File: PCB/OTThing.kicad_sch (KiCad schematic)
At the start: 68 parts, among them IC1 TPS61041, J3 USB_C_Receptacle_USB2.0, Q13 BC847C, SW1 RST/CONFIG, SW2 BOOT, U1 ESP32-C3-WROOM-02, U5 USBLC6-2SC6, U6 AMS1117-3.3

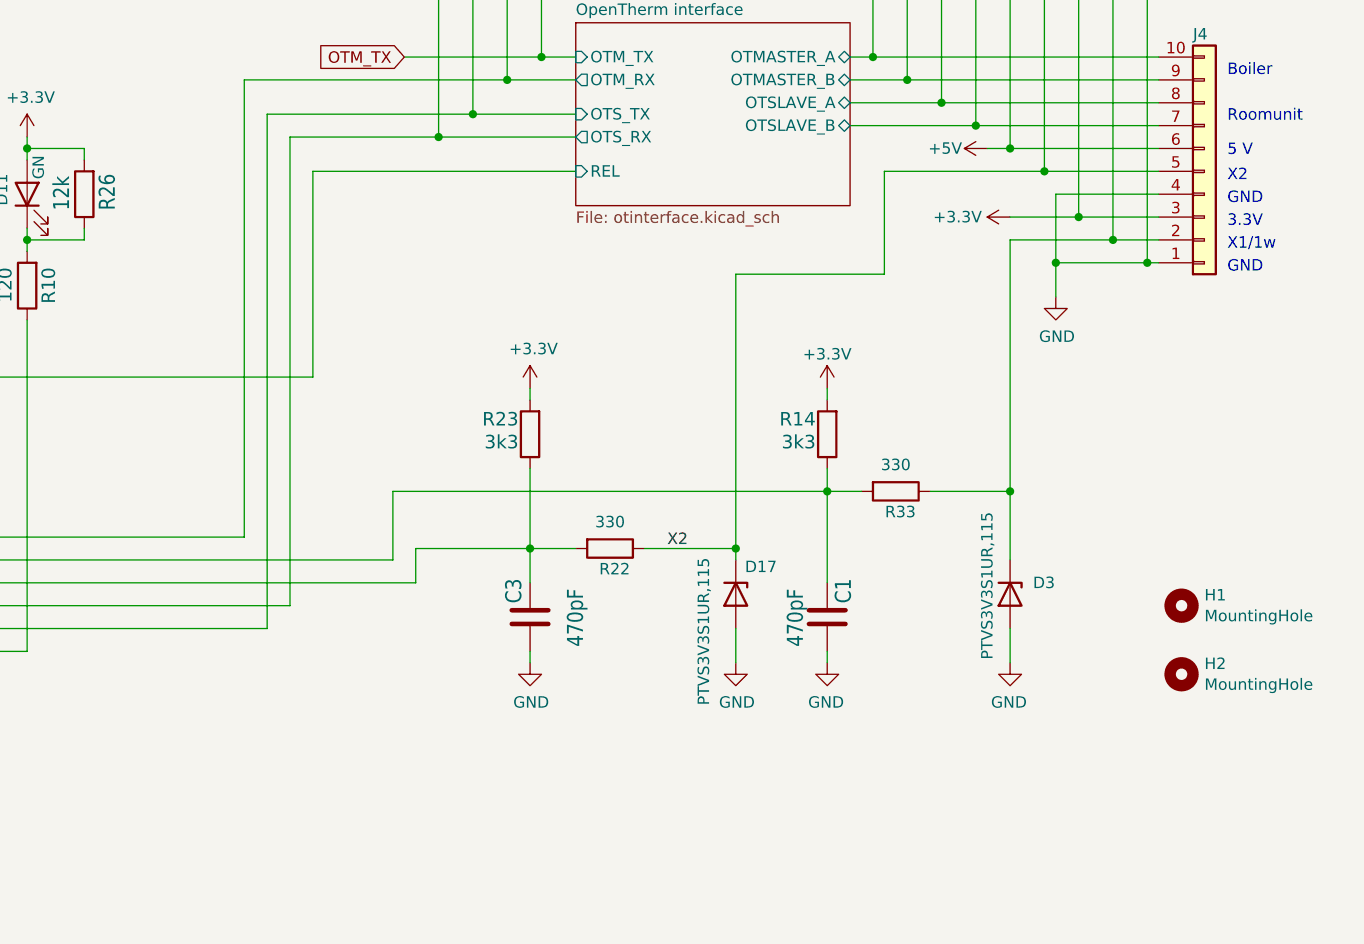
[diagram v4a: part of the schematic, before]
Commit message: add fiducals
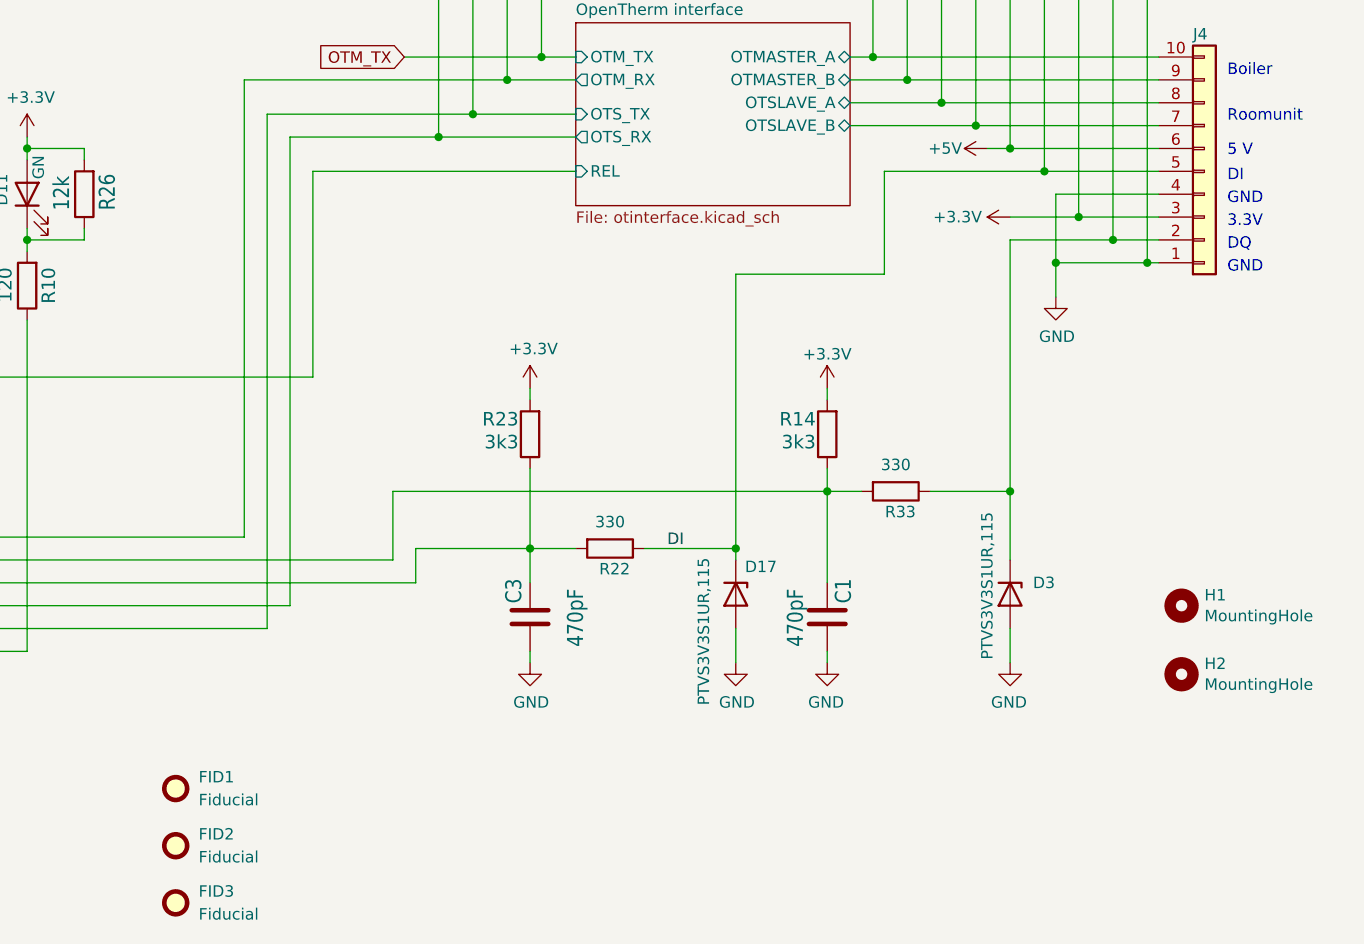
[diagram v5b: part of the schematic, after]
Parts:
- added FID1, FID2, FID3: Fiducial, Fiducial:Fiducial_0.5mm_Mask1.5mm, symbol Mechanical:Fiducial
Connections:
- net X2 renamed DI
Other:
- note added: "DI"
- note added: "DQ"
- note removed: "X1/1w"
- note removed: "X2"
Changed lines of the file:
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@@
 		)
 	)
-	(text "X1/1w"
+	(text "DQ"
 		(exclude_from_sim no)
 		(at 271.78 114.3 0)
@@
 		)
 	)
-	(text "X2"
+	(text "DI"
 		(exclude_from_sim no)
 		(at 271.78 106.68 0)
@@
 		)
 	)
-	(label "X2"
+	(label "DI"
 		(at 209.55 147.32 0)
 		(effects
@@
 	)
 	(symbol
+		(lib_id "Mechanical:Fiducial")
+		(at 154.94 173.99 0)
+		(unit 1)
+		(exclude_from_sim no)
+		(in_bom no)
+		(on_board yes)
+		(dnp no)
+		(fields_autoplaced yes)
+		(property "Reference" "FID1"
+			(at 157.48 172.7199 0)
+			(effects
+				(font
+					(size 1.27 1.27)
+				)
+				(justify left)
+			)
+		)
+		(property "Value" "Fiducial"
+			(at 157.48 175.2599 0)
+			(effects
+				(font
+					(size 1.27 1.27)
+				)
+				(justify left)
+			)
+		)
+		(property "Footprint" "Fiducial:Fiducial_0.5mm_Mask1.5mm"
+			(at 154.94 173.99 0)
+			(effects
+				(font
+					(size 1.27 1.27)
+				)
+				(hide yes)
+			)
+		)
+		(property "Datasheet" "~"
+			(at 154.94 173.99 0)
+			(effects
+				(font
+					(size 1.27 1.27)
+				)
+				(hide yes)
+			)
+		)
+		(property "Description" "Fiducial Marker"
+			(at 154.94 173.99 0)
+			(effects
+				(font
+					(size 1.27 1.27)
+				)
+				(hide yes)
+			)
+		)
+		(instances
+			(project ""
+				(path "/cb61f12f-ab02-48e5-a06c-10aea7e452c9"
+					(reference "FID1")
+					(unit 1)
+				)
+			)
+		)
+	)
+	(symbol
 		(lib_id "power:+3.3V")
 		(at 227.33 129.54 0)
@@
 	)
 	(symbol
+		(lib_id "Mechanical:Fiducial")
+		(at 154.94 186.69 0)
+		(unit 1)
+		(exclude_from_sim no)
+		(in_bom no)
+		(on_board yes)
+		(dnp no)
+		(fields_autoplaced yes)
+		(property "Reference" "FID3"
+			(at 157.48 185.4199 0)
+			(effects
+				(font
+					(size 1.27 1.27)
+				)
+				(justify left)
+			)
+		)
+		(property "Value" "Fiducial"
+			(at 157.48 187.9599 0)
+			(effects
+				(font
+					(size 1.27 1.27)
+				)
+				(justify left)
+			)
+		)
+		(property "Footprint" "Fiducial:Fiducial_0.5mm_Mask1.5mm"
+			(at 154.94 186.69 0)
+			(effects
+				(font
+					(size 1.27 1.27)
+				)
+				(hide yes)
+			)
+		)
+		(property "Datasheet" "~"
+			(at 154.94 186.69 0)
+			(effects
+				(font
+					(size 1.27 1.27)
+				)
+				(hide yes)
+			)
+		)
+		(property "Description" "Fiducial Marker"
+			(at 154.94 186.69 0)
+			(effects
+				(font
+					(size 1.27 1.27)
+				)
+				(hide yes)
+			)
+		)
+		(instances
+			(project "OTThing"
+				(path "/cb61f12f-ab02-48e5-a06c-10aea7e452c9"
+					(reference "FID3")
+					(unit 1)
+				)
+			)
+		)
+	)
+	(symbol
 		(lib_id "power:+3.3V")
 		(at 69.85 101.6 0)
@@
 					(unit 1)
 				)
+			)
+		)
+	)
+	(symbol
+		(lib_id "Mechanical:Fiducial")
+		(at 154.94 180.34 0)
+		(unit 1)
+		(exclude_from_sim no)
+		(in_bom no)
+		(on_board yes)
+		(dnp no)
+		(fields_autoplaced yes)
+		(property "Reference" "FID2"
+			(at 157.48 179.0699 0)
+			(effects
+				(font
+					(size 1.27 1.27)
+				)
+				(justify left)
+			)
+		)
+		(property "Value" "Fiducial"
+			(at 157.48 181.6099 0)
+			(effects
+				(font
+					(size 1.27 1.27)
+				)
+				(justify left)
+			)
+		)
+		(property "Footprint" "Fiducial:Fiducial_0.5mm_Mask1.5mm"
+			(at 154.94 180.34 0)
+			(effects
+				(font
+					(size 1.27 1.27)
+				)
+				(hide yes)
+			)
+		)
+		(property "Datasheet" "~"
+			(at 154.94 180.34 0)
+			(effects
+				(font
+					(size 1.27 1.27)
+				)
+				(hide yes)
+			)
+		)
+		(property "Description" "Fiducial Marker"
+			(at 154.94 180.34 0)
+			(effects
+				(font
+					(size 1.27 1.27)
+				)
+				(hide yes)
+			)
+		)
+		(instances
+			(project "OTThing"
+				(path "/cb61f12f-ab02-48e5-a06c-10aea7e452c9"
+					(reference "FID2")
+					(unit 1)
+				)

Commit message: Migrate to KiCad 10
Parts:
- FB5, J4, TP1, TP10, TP11, TP12, TP13, TP14, TP15, TP16, TP2, TP3, TP4, TP5, TP6, TP7, TP8, TP9: value ~ -> (none)

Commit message: update KiCad libraries
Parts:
- removed FID1, FID2, FID3: Fiducial, Fiducial:Fiducial_0.5mm_Mask1.5mm, symbol Mechanical:Fiducial
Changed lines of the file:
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@@
 	)
 	(symbol
-		(lib_id "Mechanical:Fiducial")
-		(at 154.94 173.99 0)
-		(unit 1)
-		(body_style 1)
-		(exclude_from_sim no)
-		(in_bom no)
-		(on_board yes)
-		(in_pos_files yes)
-		(dnp no)
-		(fields_autoplaced yes)
-		(property "Reference" "FID1"
-			(at 157.48 172.7199 0)
-			(show_name no)
-			(do_not_autoplace no)
-			(effects
-				(font
-					(size 1.27 1.27)
-				)
-				(justify left)
-			)
-		)
-		(property "Value" "Fiducial"
-			(at 157.48 175.2599 0)
-			(show_name no)
-			(do_not_autoplace no)
-			(effects
-				(font
-					(size 1.27 1.27)
-				)
-				(justify left)
-			)
-		)
-		(property "Footprint" "Fiducial:Fiducial_0.5mm_Mask1.5mm"
-			(at 154.94 173.99 0)
-			(hide yes)
-			(show_name no)
-			(do_not_autoplace no)
-			(effects
-				(font
-					(size 1.27 1.27)
-				)
-			)
-		)
-		(property "Datasheet" ""
-			(at 154.94 173.99 0)
-			(hide yes)
-			(show_name no)
-			(do_not_autoplace no)
-			(effects
-				(font
-					(size 1.27 1.27)
-				)
-			)
-		)
-		(property "Description" "Fiducial Marker"
-			(at 154.94 173.99 0)
-			(hide yes)
-			(show_name no)
-			(do_not_autoplace no)
-			(effects
-				(font
-					(size 1.27 1.27)
-				)
-			)
-		)
-		(instances
-			(project "OTThing"
-				(path "/cb61f12f-ab02-48e5-a06c-10aea7e452c9"
-					(reference "FID1")
-					(unit 1)
-				)
-			)
-		)
-	)
-	(symbol
 		(lib_id "power:+3.3V")
 		(at 227.33 129.54 0)
@@
 	)
 	(symbol
-		(lib_id "Mechanical:Fiducial")
-		(at 154.94 186.69 0)
-		(unit 1)
-		(body_style 1)
-		(exclude_from_sim no)
-		(in_bom no)
-		(on_board yes)
-		(in_pos_files yes)
-		(dnp no)
-		(fields_autoplaced yes)
-		(property "Reference" "FID3"
-			(at 157.48 185.4199 0)
-			(show_name no)
-			(do_not_autoplace no)
-			(effects
-				(font
-					(size 1.27 1.27)
-				)
-				(justify left)
-			)
-		)
-		(property "Value" "Fiducial"
-			(at 157.48 187.9599 0)
-			(show_name no)
-			(do_not_autoplace no)
-			(effects
-				(font
-					(size 1.27 1.27)
-				)
-				(justify left)
-			)
-		)
-		(property "Footprint" "Fiducial:Fiducial_0.5mm_Mask1.5mm"
-			(at 154.94 186.69 0)
-			(hide yes)
-			(show_name no)
-			(do_not_autoplace no)
-			(effects
-				(font
-					(size 1.27 1.27)
-				)
-			)
-		)
-		(property "Datasheet" ""
-			(at 154.94 186.69 0)
-			(hide yes)
-			(show_name no)
-			(do_not_autoplace no)
-			(effects
-				(font
-					(size 1.27 1.27)
-				)
-			)
-		)
-		(property "Description" "Fiducial Marker"
-			(at 154.94 186.69 0)
-			(hide yes)
-			(show_name no)
-			(do_not_autoplace no)
-			(effects
-				(font
-					(size 1.27 1.27)
-				)
-			)
-		)
-		(instances
-			(project "OTThing"
-				(path "/cb61f12f-ab02-48e5-a06c-10aea7e452c9"
-					(reference "FID3")
-					(unit 1)
-				)
-			)
-		)
-	)
-	(symbol
 		(lib_id "power:+3.3V")
 		(at 69.85 101.6 0)
@@
 	)
 	(symbol
-		(lib_id "Mechanical:Fiducial")
-		(at 154.94 180.34 0)
-		(unit 1)
-		(body_style 1)
-		(exclude_from_sim no)
-		(in_bom no)
-		(on_board yes)
-		(in_pos_files yes)
-		(dnp no)
-		(fields_autoplaced yes)
-		(property "Reference" "FID2"
-			(at 157.48 179.0699 0)
-			(show_name no)
-			(do_not_autoplace no)
-			(effects
-				(font
-					(size 1.27 1.27)
-				)
-				(justify left)
-			)
-		)
-		(property "Value" "Fiducial"
-			(at 157.48 181.6099 0)
-			(show_name no)
-			(do_not_autoplace no)
-			(effects
-				(font
-					(size 1.27 1.27)
-				)
-				(justify left)
-			)
-		)
-		(property "Footprint" "Fiducial:Fiducial_0.5mm_Mask1.5mm"
-			(at 154.94 180.34 0)
-			(hide yes)
-			(show_name no)
-			(do_not_autoplace no)
-			(effects
-				(font
-					(size 1.27 1.27)
-				)
-			)
-		)
-		(property "Datasheet" ""
-			(at 154.94 180.34 0)
-			(hide yes)
-			(show_name no)
-			(do_not_autoplace no)
-			(effects
-				(font
-					(size 1.27 1.27)
-				)
-			)
-		)
-		(property "Description" "Fiducial Marker"
-			(at 154.94 180.34 0)
-			(hide yes)
-			(show_name no)
-			(do_not_autoplace no)
-			(effects
-				(font
-					(size 1.27 1.27)
-				)
-			)
-		)
-		(instances
-			(project "OTThing"
-				(path "/cb61f12f-ab02-48e5-a06c-10aea7e452c9"
-					(reference "FID2")
-					(unit 1)
-				)
-			)
-		)
-	)
-	(symbol
 		(lib_id "power:GND")
 		(at 92.71 48.26 0)
@@
 		(pin "B9"
 		)
-		(pin "S1"
+		(pin "SH"
 		)
 		(instances
